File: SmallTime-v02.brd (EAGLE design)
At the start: 38.1 x 38.1 mm, 45 parts, among them U1 ATMEGA168, Y1 32.768kHz

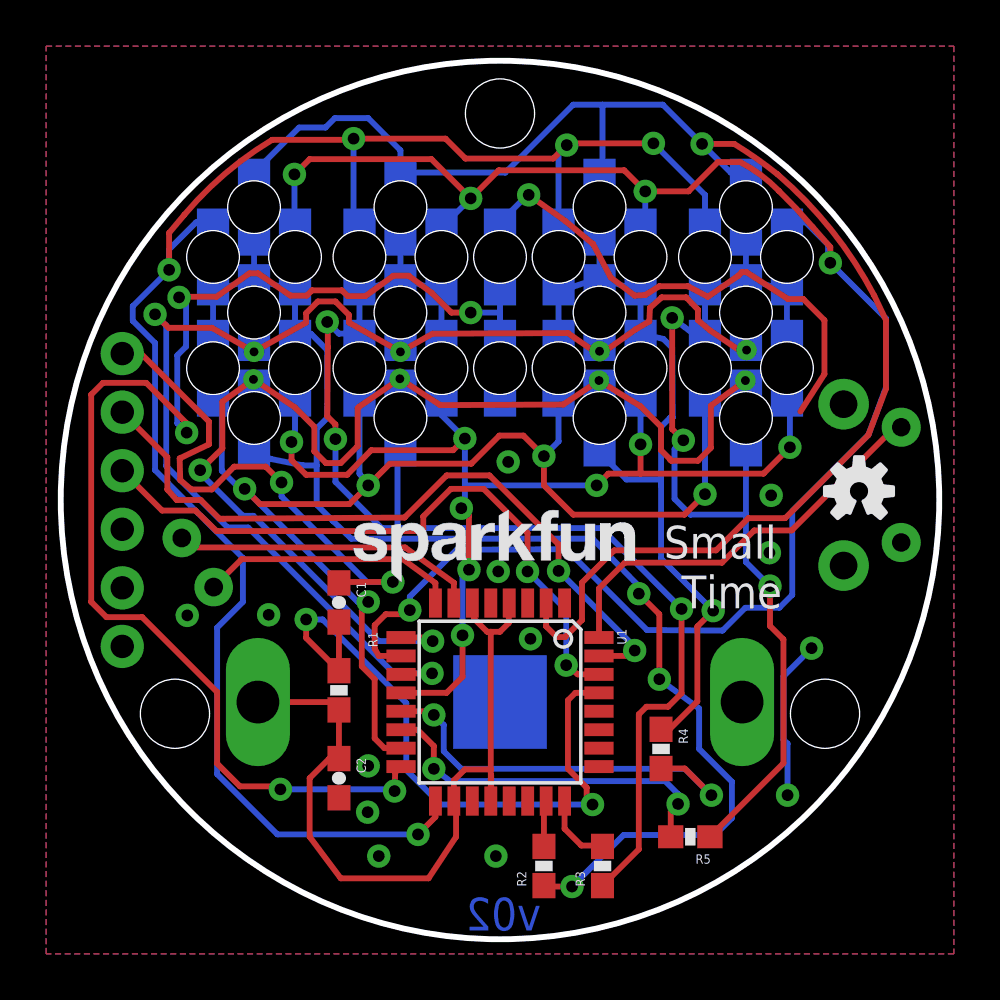
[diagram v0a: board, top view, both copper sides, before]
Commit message: Improved design
Spaced segment LEDs more evenly, moved resistors to make more clearing
for enclosure peices, cleaned up routing.
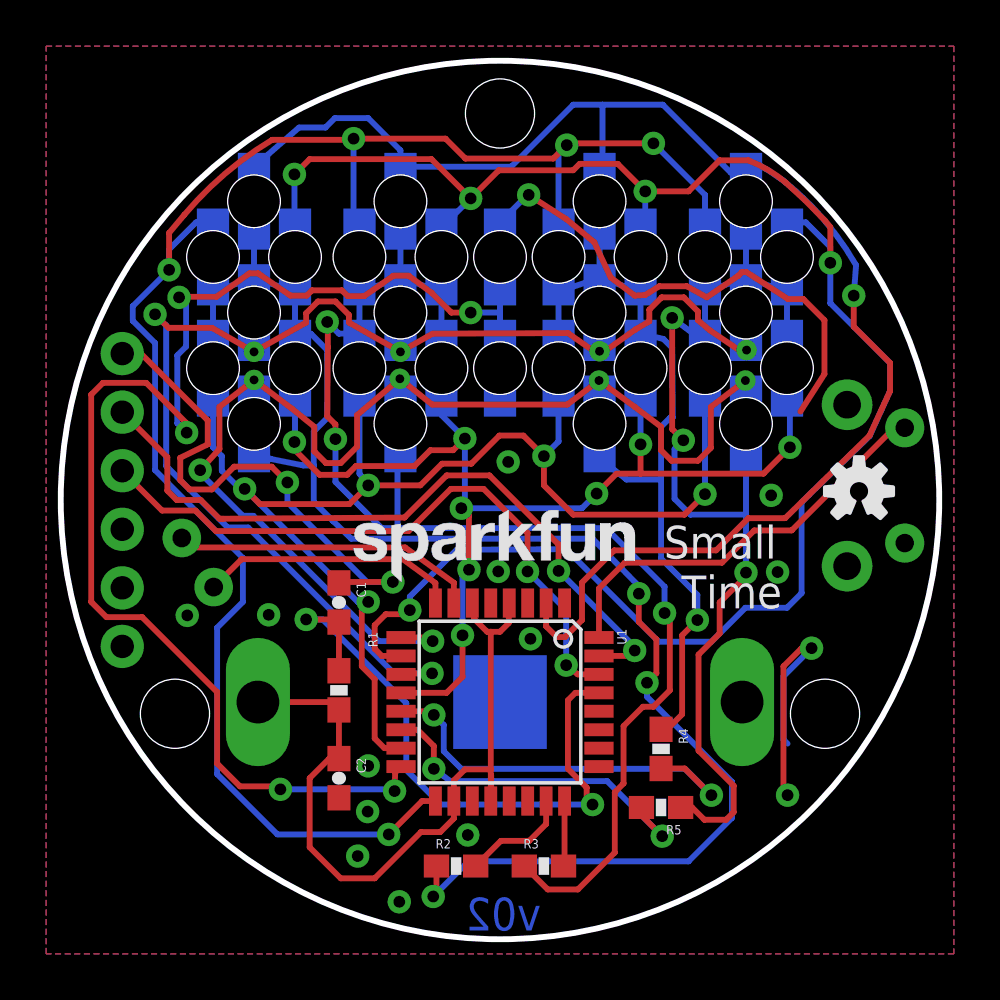
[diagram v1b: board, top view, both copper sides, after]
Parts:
- moved R2 3.81 mm to (17.8, 3.81), turned to 0 degrees
- moved R3 2.54 mm to (21.6, 3.81), turned to 0 degrees
- moved R5 1.80 mm to (26.7, 6.35)
- moved F-1 0.25 mm to (9.02, 32.6)
- moved F-2 0.25 mm to (15.4, 32.6)
- moved F-3 0.25 mm to (24.0, 32.6)
- moved F-4 0.25 mm to (30.4, 32.6)
- moved C-1 0.25 mm to (9.02, 23.0)
- moved C-2 0.25 mm to (15.4, 23.0)
- moved C-3 0.25 mm to (24.0, 23.0)
- moved C-4 0.25 mm to (30.4, 23.0)
- moved S1 0.15 mm to (37.2, 20.3)
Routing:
- net DIG1: track 57.1 -> 64.2 mm
- net GND: track 28.9 -> 34.0 mm, vias 14 -> 15
- net DIG2: track 52.3 -> 55.5 mm
- net N$7: track 2.01 -> 4.81 mm
- net F: track 65.8 -> 63.6 mm
- net A: track 77.2 -> 78.6 mm
- net RST: track 28.8 -> 27.5 mm
- net DIG4: track 41.1 -> 42.2 mm
- net C: track 51.0 -> 51.8 mm
- net VCC: track 34.4 -> 33.6 mm
- net N$6: track 3.49 -> 2.84 mm
